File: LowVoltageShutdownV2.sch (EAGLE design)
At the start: 7 parts

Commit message: second revision and added 3D models
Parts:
- removed BAT+, GND: 16G, Wire2Board:16G
- removed U$2: SISS23DN-T1-GE3CY-ND, SISS23DN-T1-GE3CT-ND:SISS23DN-T1-GE3CY-ND
- added Q1: FDD4141TO252, transistor-fet:FDD4141TO252
- added U$5, U$6: 450PAD, Wire2Board:450PAD
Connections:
- removed net BAT+: BAT+.P$1, U$1.VDD, U$2.S, U$3.CCW
- new net BAT: Q1.S, U$1.VDD, U$3.CCW, U$5.P$1
- net GND: now also U$6.P$1; no longer GND.P$1
- net N$5: now also Q1.G; no longer U$2.G
- net OUT: now also Q1.D; no longer U$2.D
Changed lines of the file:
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@@
 <part name="FRAME1" library="frames" library_urn="urn:adsk.eagle:library:229" deviceset="FRAME_A_L" device=""/>
 <part name="U$1" library="MIC842L" deviceset="MIC842L(3D_MODEL)" device="" package3d_urn="urn:adsk.eagle:package:3080138/1"/>
-<part name="U$2" library="SISS23DN-T1-GE3CT-ND" deviceset="SISS23DN-T1-GE3CY-ND" device="" package3d_urn="urn:adsk.eagle:package:3080199/2"/>
 <part name="U$3" library="trimpot" deviceset="TRIMPOT" device="" package3d_urn="urn:adsk.eagle:package:3080147/2"/>
-<part name="BAT+" library="Wire2Board" deviceset="16G" device="" package3d_urn="urn:adsk.eagle:package:3080160/3"/>
-<part name="GND" library="Wire2Board" deviceset="16G" device="" package3d_urn="urn:adsk.eagle:package:3080160/3"/>
 <part name="OUT" library="Wire2Board" deviceset="16G" device="" package3d_urn="urn:adsk.eagle:package:3080160/3"/>
 <part name="U$4" library="1655-1513-1-ND" deviceset="1655-1513-1-ND(3D_MODEL)" device="" package3d_urn="urn:adsk.eagle:package:3080154/1"/>
+<part name="U$5" library="Wire2Board" deviceset="450PAD" device="" package3d_urn="urn:adsk.eagle:package:3080342/2"/>
+<part name="U$6" library="Wire2Board" deviceset="450PAD" device="" package3d_urn="urn:adsk.eagle:package:3080342/2"/>
+<part name="Q1" library="transistor-fet" library_urn="urn:adsk.eagle:library:396" deviceset="FDD4141" device="TO252" package3d_urn="urn:adsk.eagle:package:28537/2"/>
 </parts>
 <sheets>
@@
 <instance part="FRAME1" gate="G$2" x="172.72" y="0"/>
 <instance part="U$1" gate="G$1" x="142.24" y="109.22"/>
-<instance part="U$2" gate="G$1" x="187.96" y="127"/>
 <instance part="U$3" gate="G$1" x="114.3" y="109.22" rot="R270"/>
-<instance part="BAT+" gate="G$1" x="76.2" y="147.32" rot="R180"/>
-<instance part="GND" gate="G$1" x="76.2" y="127" rot="R180"/>
 <instance part="OUT" gate="G$1" x="76.2" y="106.68" rot="R180"/>
 <instance part="U$4" gate="G$1" x="88.9" y="119.38" rot="R270"/>
+<instance part="U$5" gate="G$1" x="76.2" y="147.32" rot="R180"/>
+<instance part="U$6" gate="G$1" x="76.2" y="127" rot="R180"/>
+<instance part="Q1" gate="G$1" x="187.96" y="127"/>
 </instances>
 <busses>
@@
 </segment>
 <segment>
-<pinref part="GND" gate="G$1" pin="P$1"/>
 <wire x1="86.36" y1="127" x2="88.9" y2="127" width="0.1524" layer="91"/>
 <label x="91.44" y="127" size="1.778" layer="95" xref="yes"/>
@@
 <wire x1="88.9" y1="121.92" x2="88.9" y2="127" width="0.1524" layer="91"/>
 <junction x="88.9" y="127"/>
+<pinref part="U$6" gate="G$1" pin="P$1"/>
 </segment>
 </net>
-<net name="BAT+" class="0">
+<net name="BAT" class="0">
 <segment>
 <pinref part="U$3" gate="G$1" pin="CCW"/>
@@
 </segment>
 <segment>
-<pinref part="U$2" gate="G$1" pin="S"/>
 <wire x1="190.5" y1="132.08" x2="190.5" y2="137.16" width="0.1524" layer="91"/>
 <label x="190.5" y="137.16" size="1.778" layer="95" rot="R90" xref="yes"/>
+<pinref part="Q1" gate="G$1" pin="S"/>
 </segment>
 <segment>
-<pinref part="BAT+" gate="G$1" pin="P$1"/>
 <wire x1="86.36" y1="147.32" x2="91.44" y2="147.32" width="0.1524" layer="91"/>
 <label x="91.44" y="147.32" size="1.778" layer="95" xref="yes"/>
+<pinref part="U$5" gate="G$1" pin="P$1"/>
 </segment>
 </net>
 <net name="N$5" class="0">
 <segment>
-<pinref part="U$2" gate="G$1" pin="G"/>
 <wire x1="185.42" y1="129.54" x2="170.18" y2="129.54" width="0.1524" layer="91"/>
 <wire x1="170.18" y1="129.54" x2="170.18" y2="114.3" width="0.1524" layer="91"/>
 <pinref part="U$1" gate="G$1" pin="OUT"/>
 <wire x1="170.18" y1="114.3" x2="154.94" y2="114.3" width="0.1524" layer="91"/>
+<pinref part="Q1" gate="G$1" pin="G"/>
 </segment>
 </net>
 <net name="OUT" class="0">
 <segment>
-<pinref part="U$2" gate="G$1" pin="D"/>
 <wire x1="190.5" y1="121.92" x2="190.5" y2="116.84" width="0.1524" layer="91"/>
 <label x="190.5" y="116.84" size="1.778" layer="95" rot="R270" xref="yes"/>
+<pinref part="Q1" gate="G$1" pin="D"/>
 </segment>
 <segment>

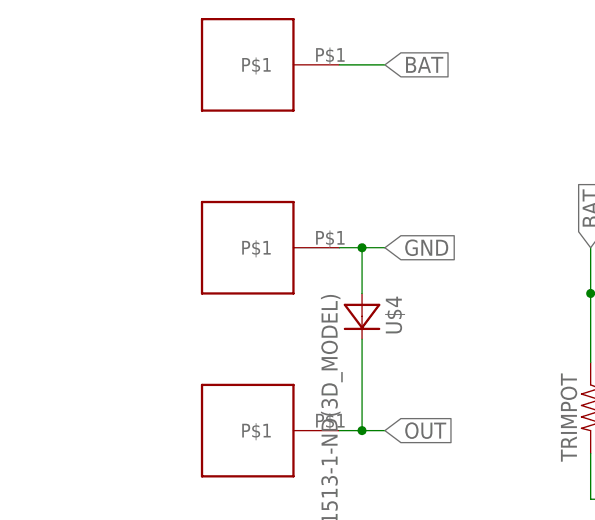
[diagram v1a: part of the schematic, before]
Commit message: added ground pin
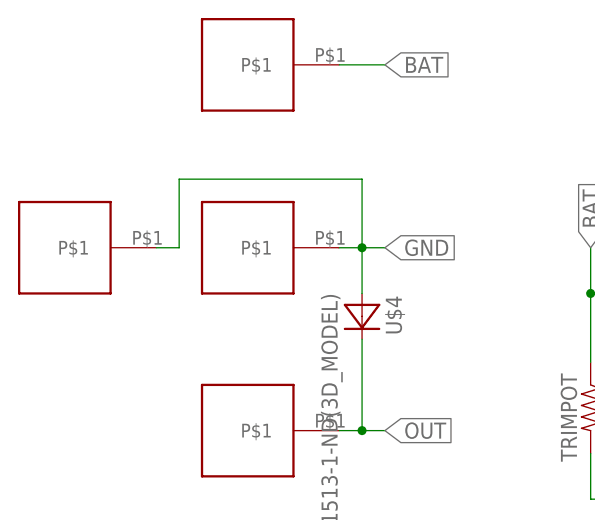
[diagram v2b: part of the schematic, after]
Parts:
- added OUT1: 16G, Wire2Board:16G
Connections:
- net GND: now also OUT1.P$1
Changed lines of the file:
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@@
 <?xml version="1.0" encoding="utf-8"?>
 <!DOCTYPE eagle SYSTEM "eagle.dtd">
-<eagle version="9.0.0">
+<eagle version="9.0.1">
 <drawing>
 <settings>
@@
 <part name="U$6" library="Wire2Board" deviceset="450PAD" device="" package3d_urn="urn:adsk.eagle:package:3080342/2"/>
 <part name="Q1" library="transistor-fet" library_urn="urn:adsk.eagle:library:396" deviceset="FDD4141" device="TO252" package3d_urn="urn:adsk.eagle:package:28537/2"/>
+<part name="OUT1" library="Wire2Board" deviceset="16G" device="" package3d_urn="urn:adsk.eagle:package:3080160/3"/>
 </parts>
 <sheets>
@@
 <instance part="U$6" gate="G$1" x="76.2" y="127" rot="R180"/>
 <instance part="Q1" gate="G$1" x="187.96" y="127"/>
+<instance part="OUT1" gate="G$1" x="55.88" y="127" rot="R180"/>
 </instances>
 <busses>
@@
 <junction x="88.9" y="127"/>
 <pinref part="U$6" gate="G$1" pin="P$1"/>
+<pinref part="OUT1" gate="G$1" pin="P$1"/>
+<wire x1="66.04" y1="127" x2="68.58" y2="127" width="0.1524" layer="91"/>
+<wire x1="68.58" y1="127" x2="68.58" y2="134.62" width="0.1524" layer="91"/>
+<wire x1="68.58" y1="134.62" x2="88.9" y2="134.62" width="0.1524" layer="91"/>
+<wire x1="88.9" y1="134.62" x2="88.9" y2="127" width="0.1524" layer="91"/>
 </segment>
 </net>
